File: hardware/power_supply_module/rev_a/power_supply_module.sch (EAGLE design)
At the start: 72 parts, among them J1 MODULE_POWER, U1 TLV62130, U10 LTC2941, U11 LTC2941, U12 LTC2941, U13 TLV62130, U14 PCA9544A, U15 LTC2941, U2 PCA9544A, U3 LTC2941, U4 LTC2941, U5 LTC2941, U6 TLV62130, U7 TLV62130, U8 LTC2941, U9 TLV62130

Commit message: Power Module Board Layout
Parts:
- removed C31, C32, C33, C54, C55, C56: 0.1u, passives:CAPACITOR0402_CAP
- removed C42: 0.1uF, passives:CAPACITOR0402_CAP
- removed C43: 3.3nF, passives:CAPACITOR0402_CAP
- removed L6: 2.2uH, passives:INDUCTORIHL
- removed R28, R29, R30, R31, R32, R33: 0.017, passives:RESISTOR0805_RES
- removed R35: 240k, passives:RESISTOR0402_RES
- removed R36: 100K, passives:RESISTOR0402_RES
- added C20, C21, C22, C23: 10uF, passives:CAPACITOR0402_CAP
- added C25, C26, C27, C28: 22uF, passives:CAPACITOR0402_CAP
- added L5: 2.2uH, passives:INDUCTORIHL
- added R13: 100K, passives:RESISTOR0402_RES
- added R14, R15, R16, R17: 143k, passives:RESISTOR0402_RES
- added R20, R21, R22: 750k, passives:RESISTOR0402_RES
- C1, C5: value 10uF -> 3.3nF
- C11, C15: value 3.3nF -> 0.1u
- C12, C16: value 22uF -> 0.1u
- C13: value 10uF -> 0.1u
- C14: value 0.1uF -> 0.1u
- C2: value 0.1uF -> 3.3nF
- C4: value 22uF -> 3.3nF
- C7: value 3.3nF -> 0.1uF
- C8: value 22uF -> 0.1uF
- C9: value 10uF -> 0.1uF
- R1, R4, R7: value 750k -> 0.017; device passives:RESISTOR0402_RES -> passives:RESISTOR0805_RES
- R10: value 750k -> 100K
- R11: value 143k -> 100K
- R18: value 0.017 -> 240k; device passives:RESISTOR0805_RES -> passives:RESISTOR0402_RES
- R2, R5, R8: value 143k -> 0.017; device passives:RESISTOR0402_RES -> passives:RESISTOR0805_RES
- R23: value 0.017 -> 750k; device passives:RESISTOR0805_RES -> passives:RESISTOR0402_RES
- R3, R6: value 100K -> 0.017; device passives:RESISTOR0402_RES -> passives:RESISTOR0805_RES
- U13, U9: value TLV62130 -> LTC2941; device chips:TLV62130 -> signpost:LTC2941
- U14: value PCA9544A -> LTC2941; device signpost:PCA9544A -> signpost:LTC2941
- U2: value PCA9544A -> TLV62130; device signpost:PCA9544A -> chips:TLV62130
- U3, U4, U5: value LTC2941 -> TLV62130; device signpost:LTC2941 -> chips:TLV62130
- U6, U7: value TLV62130 -> PCA9544A; device chips:TLV62130 -> signpost:PCA9544A
- renumbered C34 to C17, C40 to C18, C41 to C19, C57 to C24, R34 to R19
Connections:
- removed net N$62 (its old number): L6.1, U6.SW
- new net N$6: L3.1, U3.SW
- net !INT: now also U6.!INT, U7.!INT; no longer U14.!INT, U2.!INT
- net 3V3: now also L1.2, R1.2, R9.2, U1.VOS, U8.SENSE+; no longer L6.2, R33.2, R36.2, U15.SENSE+, U6.VOS
- net 5V_1: now also C26.2, L3.2, R11.2, R2.2, R21.2, U3.VOS, U9.SENSE+; no longer C4.2, L1.2, R1.2, R18.2, R28.2, R3.2, U1.VOS, U3.SENSE+, U4.SENSE+
- net 5V_2: now also C25.2, R10.2, R20.2, R3.2, U10.SENSE+, U11.SENSE+, U2.VOS; no longer C8.2, R29.2, R30.2, R6.2, U5.SENSE+, U7.VOS, U8.SENSE+
- net 5V_3: now also C27.2, L4.2, R12.2, R22.2, R5.2, R6.2, U12.SENSE+, U13.SENSE+, U4.VOS; no longer C12.2, L3.2, R23.2, R31.2, R7.2, R9.2, U10.SENSE+, U11.SENSE+, U9.VOS
- net 5V_4: now also C28.2, L5.2, R13.2, R23.2, R7.2, R8.2, U14.SENSE+, U15.SENSE+, U5.VOS; no longer C16.2, L4.2, R10.2, R12.2, R32.2, U12.SENSE+, U13.VOS
- net GND: now also C1.1, C11.2, C12.2, C15.2, C16.2, C2.1, C20.2, C21.2, C22.2, C23.2, C25.1, C26.1, C27.1, C28.1, C5.1, C7.2, C8.2, R14.1, R15.1, R16.1, R17.1, R18.1, U13.GND, U2.AGND, U2.DEF, U2.FSW, U2.PGND, U3.AGND, U3.DEF, U3.FSW, U3.PGND, U4.AGND, U4.DEF, U4.FSW, U4.PGND, U5.AGND, U5.DEF, U5.FSW, U5.PGND, U6.A0, U6.A1, U6.A2, U6.GND, U7.A1, U7.A2, U7.GND, U9.GND; no longer C1.2, C11.1, C12.1, C15.1, C16.1, C2.2, C31.2, C32.2, C33.2, C42.2, C43.1, C5.2, C54.2, C55.2, C56.2, C7.1, C8.1, R11.1, R2.1, R35.1, R5.1, R8.1, U13.AGND, U13.DEF, U13.FSW, U13.PGND, U14.A0, U14.A1, U14.A2, U2.A1, U2.A2, U2.GND, U3.GND, U4.GND, U5.GND, U6.AGND, U6.DEF, U6.FSW, U6.PGND, U7.AGND, U7.DEF, U7.FSW, U7.PGND, U9.AGND, U9.DEF, U9.FSW, U9.PGND
- net N$1: now also C2.2, U2.SS/TR; no longer C7.2, U7.SS/TR
- net N$10: now also L4.1, U4.SW; no longer L3.1, U9.SW
- net N$11: now also R12.1, U4.PG; no longer R9.1, U9.PG
- net N$12: now also R16.2, R22.1, U4.FB; no longer R7.1, R8.2, U9.FB
- net N$13: now also C5.2, U5.SS/TR; no longer C15.2, U13.SS/TR
- net N$14: now also L5.1, U5.SW; no longer L4.1, U13.SW
- net N$15: now also R13.1, U5.PG; no longer R12.1, U13.PG
- net N$16: now also R17.2, R23.1, U5.FB; no longer R10.1, R11.2, U13.FB
- net N$2: now also U2.SW; no longer U7.SW
- net N$21: now also U12.SDA, U7.SD0; no longer U10.SDA, U2.SD0
- net N$22: now also U12.SCL, U7.SC0; no longer U10.SCL, U2.SC0
- net N$23: now also U14.SDA, U7.SD2; no longer U12.SDA, U2.SD2
- net N$24: now also U14.SCL, U7.SC2; no longer U12.SCL, U2.SC2
- net N$25: now also U14.!ALERT, U7.!INT2; no longer U12.!ALERT, U2.!INT2
- net N$26: now also U7.SD3; no longer U2.SD3
- net N$27: now also U7.SC3; no longer U2.SC3
- net N$3: now also R10.1, U2.PG; no longer R6.1, U7.PG
- net N$4: now also R14.2, R20.1, U2.FB; no longer R4.1, R5.2, U7.FB
- net N$43: now also U6.SD0, U8.SDA; no longer U14.SD0, U3.SDA
- net N$46: now also U7.!INT3; no longer U2.!INT3
- net N$47: now also U6.SC0, U8.SCL; no longer U14.SC0, U3.SCL
- net N$48: now also U12.!ALERT, U7.!INT0; no longer U10.!ALERT, U2.!INT0
- net N$49: now also U13.SDA, U7.SD1; no longer U11.SDA, U2.SD1
- net N$5: now also U3.SS/TR; no longer U1.SS/TR
- net N$50: now also U13.SCL, U7.SC1; no longer U11.SCL, U2.SC1
- net N$51: now also U13.!ALERT, U7.!INT1; no longer U11.!ALERT, U2.!INT1
- net N$52: now also U10.SDA, U6.SD2; no longer U14.SD2, U5.SDA
- net N$53: now also U10.SCL, U6.SC2; no longer U14.SC2, U5.SCL
- net N$54: now also U10.!ALERT, U6.!INT2; no longer U14.!INT2, U5.!ALERT
- net N$55: now also U11.SDA, U6.SD3; no longer U14.SD3, U8.SDA
- net N$56: now also U11.SCL, U6.SC3; no longer U14.SC3, U8.SCL
- net N$57: now also U11.!ALERT, U6.!INT3; no longer U14.!INT3, U8.!ALERT
- net N$61: now also C1.2, U1.SS/TR; no longer C43.2, U6.SS/TR
- net N$63: now also R9.1, U1.PG; no longer R36.1, U6.PG
- net N$64: now also R18.2, U1.FB; no longer R35.2, U6.FB
- net N$67: now also U6.!INT0, U8.!ALERT; no longer U14.!INT0, U3.!ALERT
- net N$68: now also U6.SD1, U9.SDA; no longer U14.SD1, U4.SDA
- net N$7: now also R11.1, U3.PG; no longer R3.1, U1.PG
- net N$70: now also U6.SC1, U9.SCL; no longer U14.SC1, U4.SCL
- net N$71: now also U6.!INT1, U9.!ALERT; no longer U14.!INT1, U4.!ALERT
- net N$8: now also C4.2, U4.SS/TR; no longer C11.2, U9.SS/TR
- net N$9: now also R15.2, R21.1, U3.FB; no longer R1.1, R2.2, U1.FB
- net SCL: now also U6.SCL, U7.SCL; no longer U14.SCL, U2.SCL
- net SDA: now also U6.SDA, U7.SDA; no longer U14.SDA, U2.SDA
- net VBATT: now also C20.1, C21.1, C22.1, C23.1, C7.1, C8.1, U2.AVIN, U2.EN, U2.PVIN, U3.AVIN, U3.EN, U3.PVIN, U4.AVIN, U4.EN, U4.PVIN, U5.AVIN, U5.EN, U5.PVIN; no longer C1.1, C13.1, C14.1, C2.1, C42.1, C5.1, U13.AVIN, U13.EN, U13.PVIN, U6.AVIN, U6.EN, U6.PVIN, U7.AVIN, U7.EN, U7.PVIN, U9.AVIN, U9.EN, U9.PVIN
- net VCC_BACKPLANE: now also C11.1, R1.1, U6.VCC, U7.A0, U7.VCC, U8.SENSE-; no longer C18.1, R33.1, U14.VCC, U15.SENSE-, U2.A0, U2.VCC
- net VCC_LINUX: now also C12.1, R2.1, U9.SENSE-; no longer C17.1, R32.1, U12.SENSE-
- net VCC_MOD0: now also C13.1, R3.1, U10.SENSE-; no longer C31.1, R18.1, U3.SENSE-
- net VCC_MOD1: now also C14.1, R4.1, U11.SENSE-; no longer C54.1, R28.1, U4.SENSE-
- net VCC_MOD2: now also C15.1, R5.1, U12.SENSE-; no longer C55.1, R29.1, U5.SENSE-
- net VCC_MOD5: now also C16.1, R6.1, U13.SENSE-; no longer C56.1, R30.1, U8.SENSE-
- net VCC_MOD6: now also C17.1, R7.1, U14.SENSE-; no longer C32.1, R23.1, U10.SENSE-
- net VCC_MOD7: now also C18.1, R8.1, U15.SENSE-; no longer C33.1, R31.1, U11.SENSE-
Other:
- note added: "For MOD0-2,5"
- note removed: "For MOD0, MOD1, MOD2, MOD5"

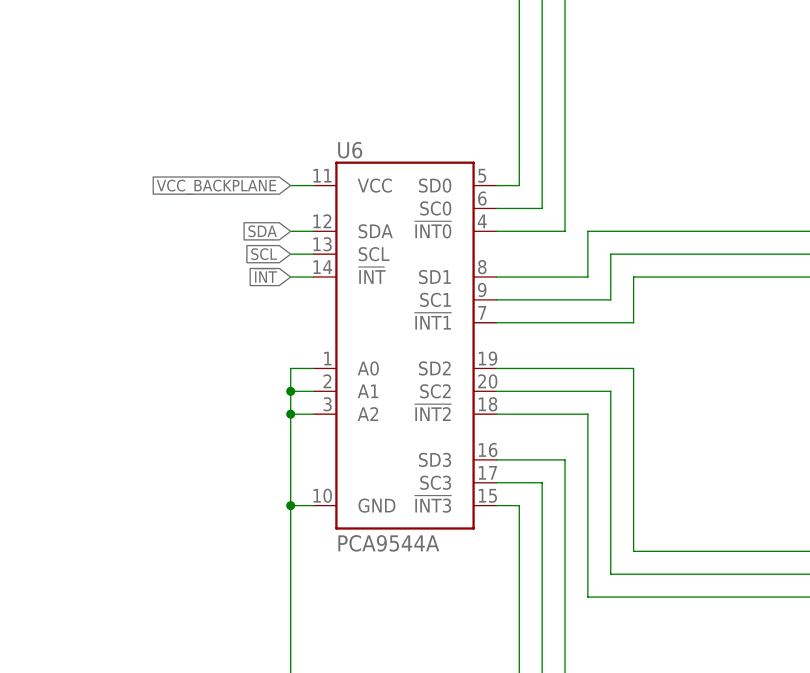
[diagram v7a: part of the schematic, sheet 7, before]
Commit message: Fixes to PCA9544A, add thermal pads to LTC2941, TLV62430.
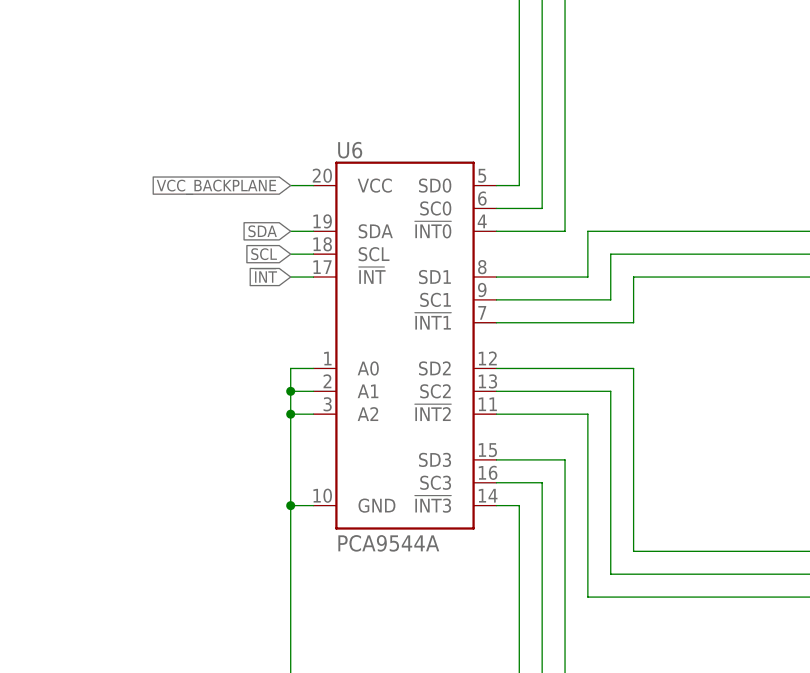
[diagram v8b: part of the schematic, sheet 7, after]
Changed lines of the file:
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@@
 <?xml version="1.0" encoding="utf-8"?>
 <!DOCTYPE eagle SYSTEM "eagle.dtd">
-<eagle version="6.6.0">
+<eagle version="6.5.0">
 <drawing>
 <settings>
